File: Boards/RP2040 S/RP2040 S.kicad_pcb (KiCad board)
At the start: 4 copper layers, 60 x 22 mm, 8 parts, among them J1 Conn_01x20_Socket, J3 Conn_01x05_Socket, J5 Conn_01x05_Socket, J6 Conn_01x05_Socket, J7 Conn_01x01_Socket, J8 Conn_01x01_Socket, J9 Conn_01x01_Socket

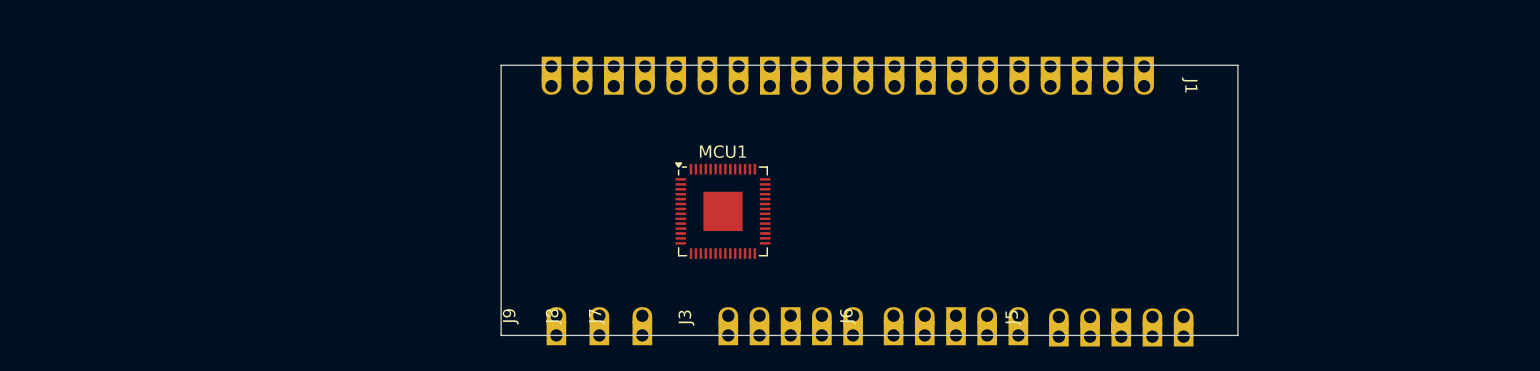
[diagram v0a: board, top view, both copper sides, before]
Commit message: RP2040 FOOTPRINTS
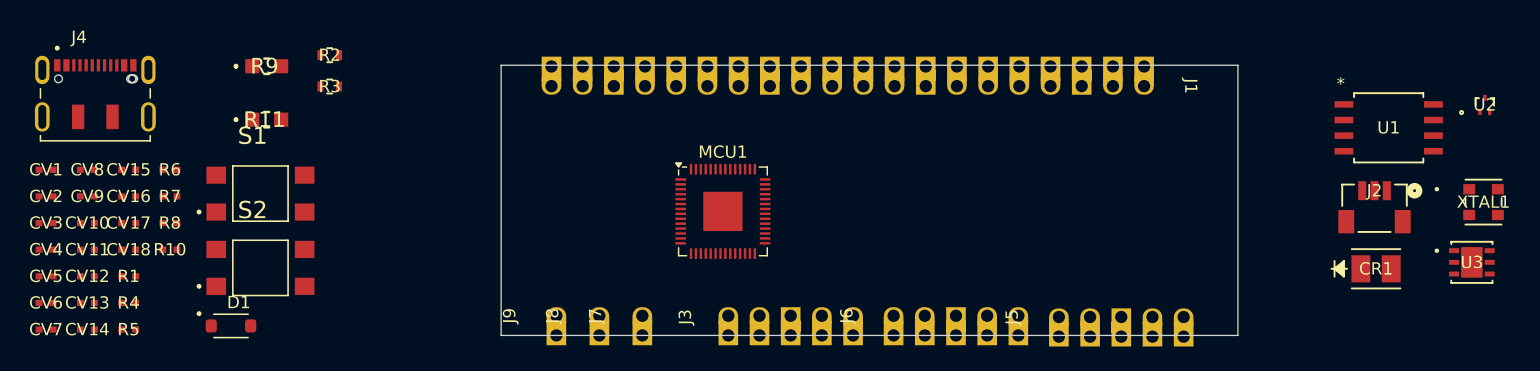
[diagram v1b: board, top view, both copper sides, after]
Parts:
- added CR1: VLMC3100-GS08, LED-Green_VLMC3100-GS08:LED_PLCC_VSMB, F.Cu at (183.2, 72.6)
- added CV1: 1uF, Capacitor-0402:Capacitor_0402, F.Cu at (74.9, 64.5)
- added CV10: 100nF, Capacitor-0402:Capacitor_0402, F.Cu at (78.3, 68.8)
- added CV11: 100nF, Capacitor-0402:Capacitor_0402, F.Cu at (78.3, 71.0)
- added CV12: 100nF, Capacitor-0402:Capacitor_0402, F.Cu at (78.3, 73.2)
- added CV13: 1uF, Capacitor-0402:Capacitor_0402, F.Cu at (78.3, 75.4)
- added CV14: 100nF, Capacitor-0402:Capacitor_0402, F.Cu at (78.3, 77.5)
- added CV15: 4.7uF, Capacitor-0402:Capacitor_0402, F.Cu at (81.7, 64.5)
- added CV16: 4.7uF, Capacitor-0402:Capacitor_0402, F.Cu at (81.7, 66.7)
- added CV17: 1uF, Capacitor-0402:Capacitor_0402, F.Cu at (81.7, 68.8)
- added CV18: 100nF, Capacitor-0402:Capacitor_0402, F.Cu at (81.7, 71.0)
- added CV2: 100nF, Capacitor-0402:Capacitor_0402, F.Cu at (74.9, 66.7)
- added CV3: 1uF, Capacitor-0402:Capacitor_0402, F.Cu at (74.9, 68.8)
- added CV4: 100nF, Capacitor-0402:Capacitor_0402, F.Cu at (74.9, 71.0)
- added CV5: 100nF, Capacitor-0402:Capacitor_0402, F.Cu at (74.9, 73.2)
- added CV6: 1uF, Capacitor-0402:Capacitor_0402, F.Cu at (74.9, 75.4)
- added CV7: 100nF, Capacitor-0402:Capacitor_0402, F.Cu at (74.9, 77.5)
- added CV8: 100nF, Capacitor-0402:Capacitor_0402, F.Cu at (78.3, 64.5)
- added CV9: 100nF, Capacitor-0402:Capacitor_0402, F.Cu at (78.3, 66.7)
- added D1: PMEG2010ER, Diode-Schottky_PMEG2010ER:SODFL3517X110N, F.Cu at (90.0, 77.2)
- added J2: BM03B-SRSS-TBLFSN, SWD_Con:CONN_BM03B-SRSS-TBLFSN_JST, F.Cu at (183.1, 67.6)
- added J4: DX07S016JA1R1500, USBC-DX07S016JA1:JAE_DX07S016JA1R1500, F.Cu at (79.0, 57.1)
- added R1: 1k, Capacitor-0402:Capacitor_0402, F.Cu at (81.7, 73.2)
- added R10: 1k, Capacitor-0402:Capacitor_0402, F.Cu at (85.0, 71.0)
- added R11: 5k1, Resistor-0805:R_0805_5K1, F.Cu at (92.9, 60.4)
- added R2: 27, Resistor-0603:RES_R0603_27, F.Cu at (98.0, 55.2)
- added R3: 27, Resistor-0603:RES_R0603_27, F.Cu at (98.0, 57.7)
- added R4: 100, Capacitor-0402:Capacitor_0402, F.Cu at (81.7, 75.4)
- added R5: 100, Capacitor-0402:Capacitor_0402, F.Cu at (81.7, 77.5)
- added R6: 1k, Capacitor-0402:Capacitor_0402, F.Cu at (85.0, 64.5)
- added R7: 10k, Capacitor-0402:Capacitor_0402, F.Cu at (85.0, 66.7)
- added R8: 665, Capacitor-0402:Capacitor_0402, F.Cu at (85.0, 68.8)
- added R9: 5k1, Resistor-0805:R_0805_5K1, F.Cu at (92.9, 56.1)
- added S1: TL3305CF160QG, E-Switch_7mm:SW_TL3305CF160QG, F.Cu at (92.4, 66.5)
- added S2: TL3305CF160QG, E-Switch_7mm:SW_TL3305CF160QG, F.Cu at (92.4, 72.5)
- added U1: W25Q128JVSIQ TR, NOR Flash:SOIC_208MIL_WIN, F.Cu at (184.3, 61.1)
- added U2: ESD7L5.0DT5G, ESD7L5-Diode:SOT-723_0P85X1P25_ONS, F.Cu at (192.1, 59.2)
- added U3: ST1L05APU33R, LDO ST1L05A:DFN_5APU33R_STM, F.Cu at (191.1, 72.0)
- added XTAL1: ASE-12.000MHZ-LC-T, AS12MHz:ASE-3.2X2.5_ABR, F.Cu at (192.0, 67.1)

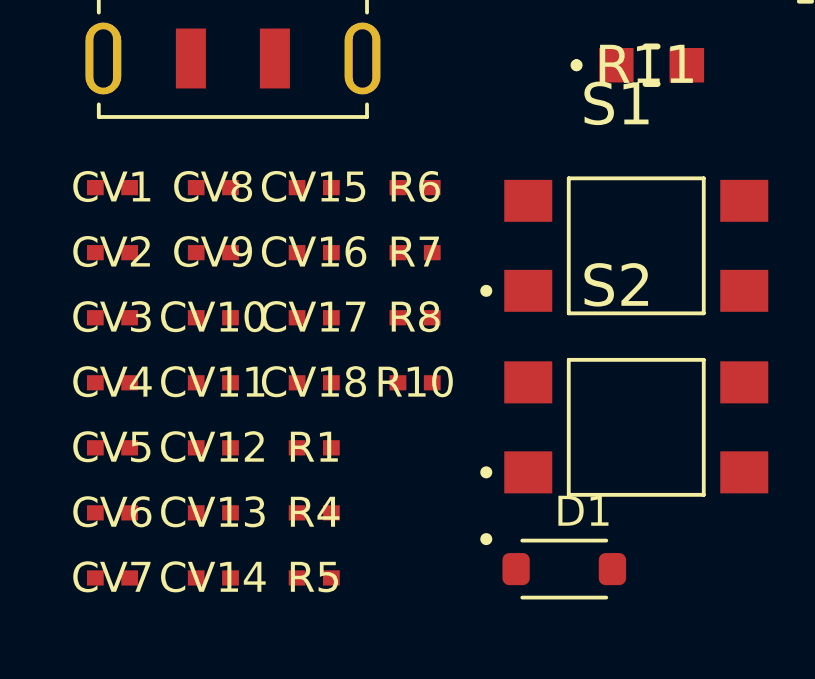
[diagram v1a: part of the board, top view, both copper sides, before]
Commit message: Footprints (RP2040 Corrigido e OBC)
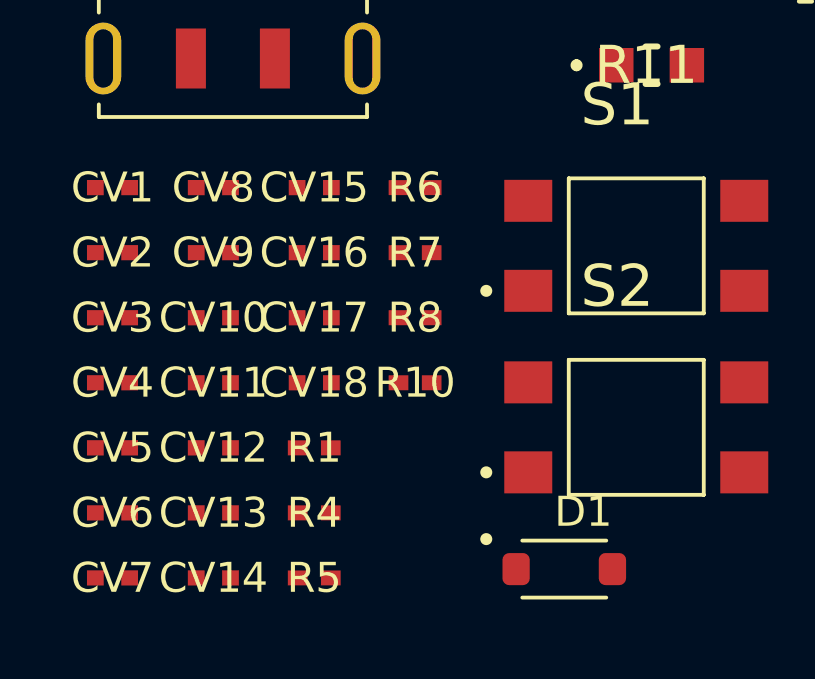
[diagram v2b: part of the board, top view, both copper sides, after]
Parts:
- R1, R10, R4, R5, R6, R7, R8: footprint Capacitor-0402:Capacitor_0402 -> Resistor-0402:RES_0402

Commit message: Mudanças nas Schematics
- Capacitor-0805 adicionado à library
- Nomes de Passive Components atualizados na library
- Atualizado as footprint dos RP2040 S, OBC, R COMMS
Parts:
- R11, R9: footprint Resistor-0805:R_0805_5K1 -> Resistor-0805:RES_0805
- R2, R3: footprint Resistor-0603:RES_R0603_27 -> Resistor-0603:RES_0603
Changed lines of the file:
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@@
 		)
 	)
-	(footprint "Resistor-0805:R_0805_5K1"
+	(footprint "Resistor-0805:RES_0805"
 		(layer "F.Cu")
 		(at 92.91 60.43)
@@
 			)
 		)
-		(property "Footprint" "Resistor-0805:R_0805_5K1"
+		(property "Footprint" "Resistor-0805:RES_0805"
 			(at 0 0 0)
 			(layer "F.Fab")
@@
 		)
 	)
-	(footprint "Resistor-0603:RES_R0603_27"
+	(footprint "Resistor-0603:RES_0603"
 		(layer "F.Cu")
 		(at 98.0402 55.1797)
@@
 			)
 		)
-		(property "Footprint" "Resistor-0603:RES_R0603_27"
+		(property "Footprint" "Resistor-0603:RES_0603"
 			(at 0 0 0)
 			(layer "F.Fab")
@@
 		)
 	)
-	(footprint "Resistor-0603:RES_R0603_27"
+	(footprint "Resistor-0603:RES_0603"
 		(layer "F.Cu")
 		(at 98.0402 57.7291)
@@
 			)
 		)
-		(property "Footprint" "Resistor-0603:RES_R0603_27"
+		(property "Footprint" "Resistor-0603:RES_0603"
 			(at 0 0 0)
 			(layer "F.Fab")
@@
 		)
 	)
-	(footprint "Resistor-0805:R_0805_5K1"
+	(footprint "Resistor-0805:RES_0805"
 		(layer "F.Cu")
 		(at 92.91 56.08)
@@
 			)
 		)
-		(property "Footprint" "Resistor-0805:R_0805_5K1"
+		(property "Footprint" "Resistor-0805:RES_0805"
 			(at 0 0 0)
 			(layer "F.Fab")
